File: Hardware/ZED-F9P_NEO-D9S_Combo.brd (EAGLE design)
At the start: 43.2 x 63.5 mm, 179 parts, among them J1 ANTENNA-SMA-GROUNDEDEDGE_SMA, J2 Qwiic Right Angle, J4 Qwiic Right Angle, U1 U-BLOX_NEO-D9S-00B, U2 3.3V, U4 U-BLOX_ZED-F9P, U5 ESD Diode, U6 ESD Diode

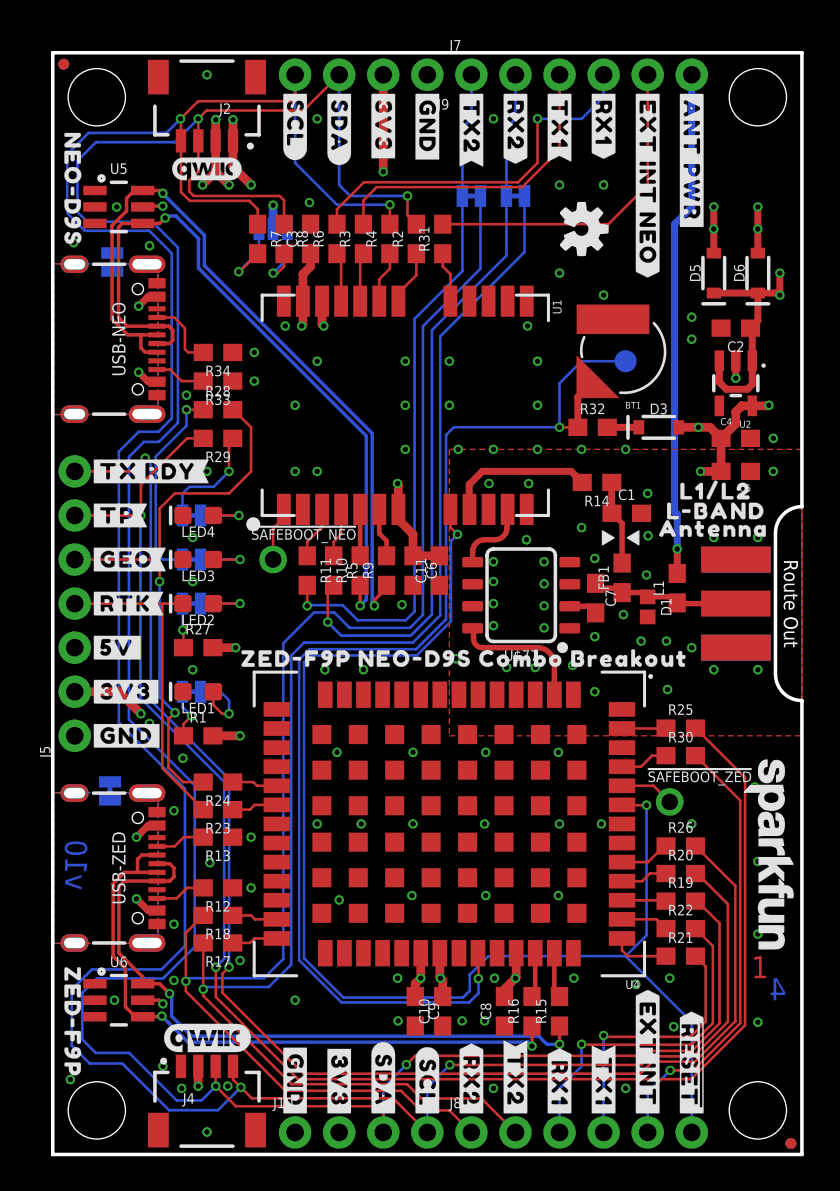
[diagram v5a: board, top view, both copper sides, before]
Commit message: Adds a few vias, fixes some ground pour
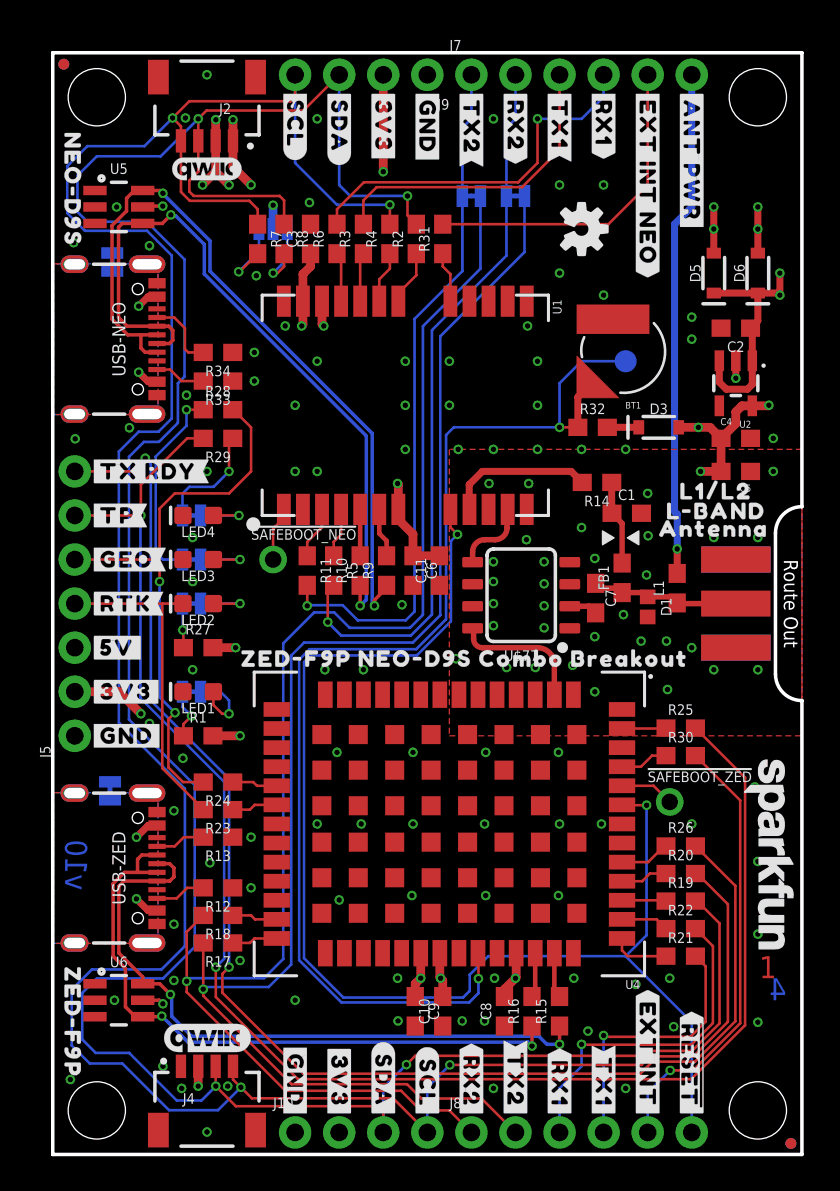
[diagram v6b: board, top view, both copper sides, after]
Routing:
- net GND: vias 123 -> 128

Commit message: Updates note for USB 90 Ohm impedance calculation
* Moves all silk out towards the PTH's
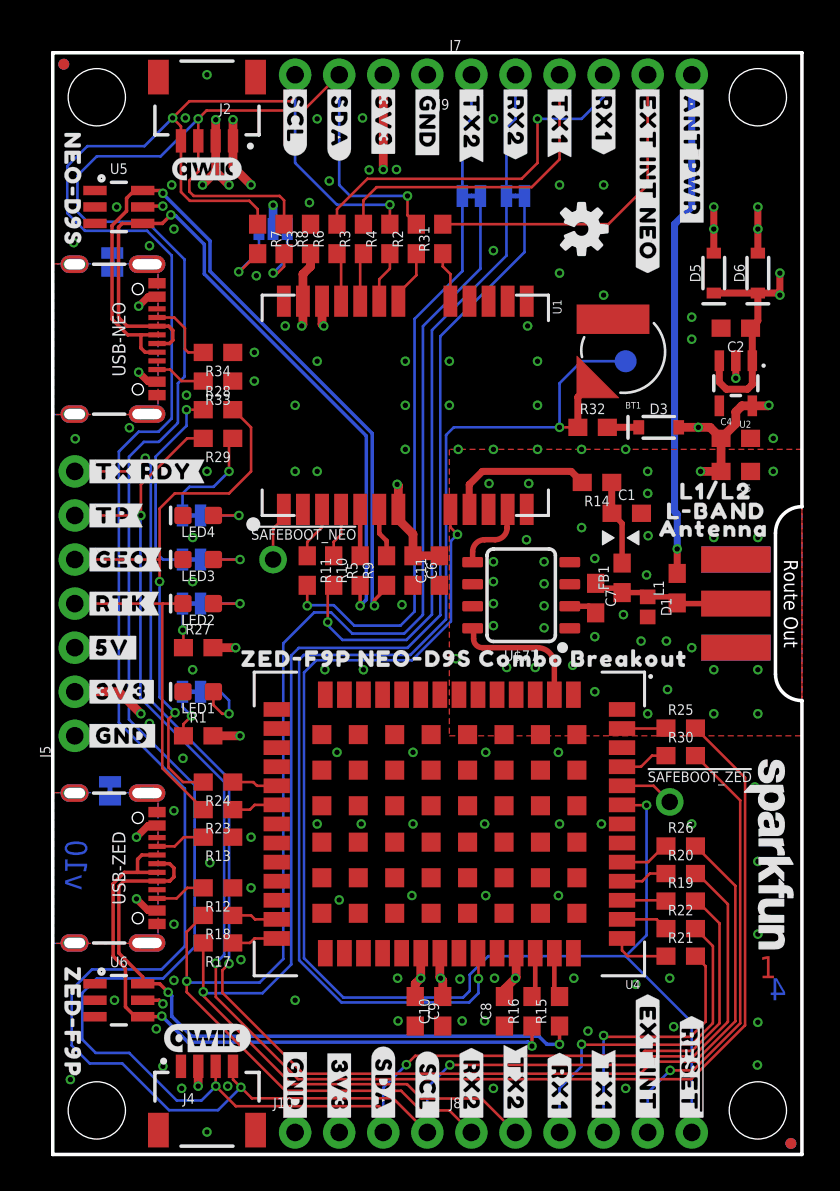
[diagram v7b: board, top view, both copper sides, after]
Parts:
- moved U$10 0.25 mm to (19.1, 1.78)
- moved U$11 0.25 mm to (19.1, 1.78)
- moved U$16 0.25 mm to (1.78, 31.8)
- moved U$17 0.25 mm to (1.78, 31.8)
- moved U$18 0.25 mm to (1.78, 34.3)
- moved U$19 0.25 mm to (1.78, 34.3)
- moved U$2 0.25 mm to (1.78, 24.1)
- moved U$20 0.25 mm to (1.78, 29.2)
- moved U$21 0.25 mm to (1.78, 29.2)
- moved U$23 0.25 mm to (16.5, 1.78)
- moved U$25 0.25 mm to (16.5, 1.78)
- moved U$26 0.25 mm to (1.78, 36.8)
- moved U$27 0.25 mm to (1.78, 36.8)
- moved U$28 0.25 mm to (1.78, 39.4)
- moved U$29 0.25 mm to (1.78, 39.4)
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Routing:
- net GND: vias 128 -> 142

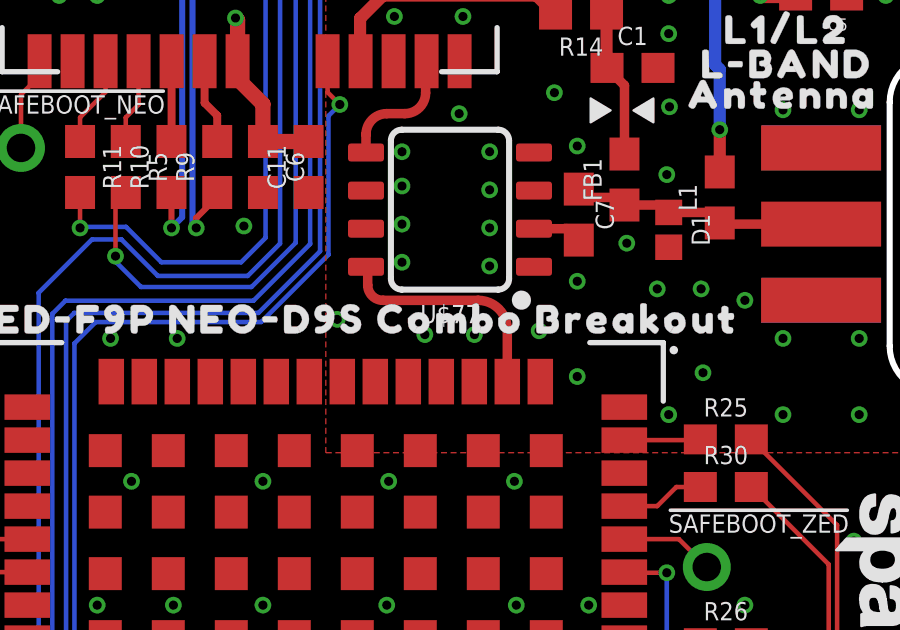
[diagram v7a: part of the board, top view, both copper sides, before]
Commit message: Updates BP2G1+ with minor corrections
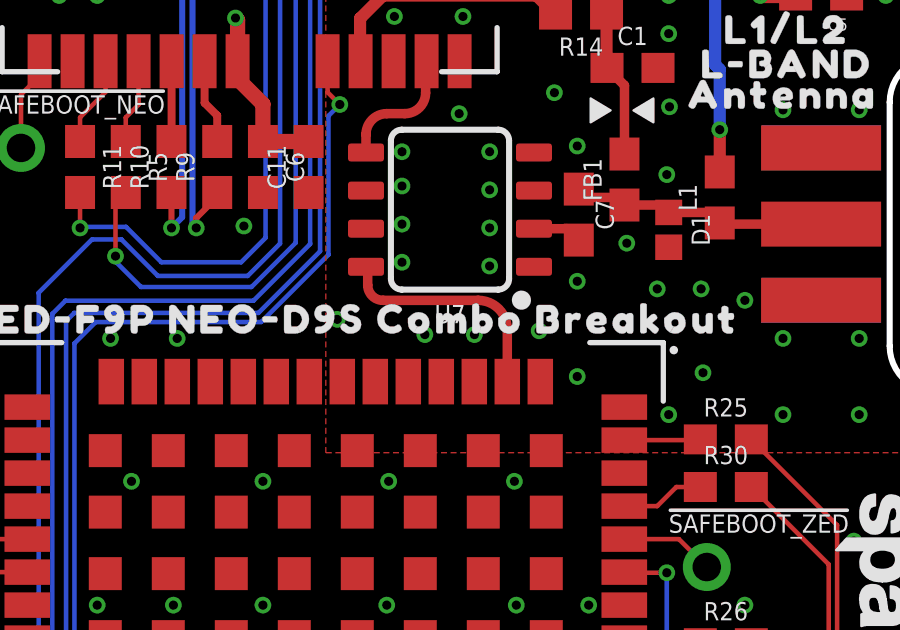
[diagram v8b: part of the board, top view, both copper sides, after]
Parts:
- renumbered U$77 to U7
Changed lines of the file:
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@@
 <attribute name="VALUE" x="3.81" y="6.35" size="0.6096" layer="27" font="vector" ratio="20" align="bottom-center"/>
 </element>
-<element name="U$77" library="SparkFun-RF" package="XX21" value="BP2G1+_POWER_SPLITTER" x="27.0002" y="32.2326" smashed="yes" rot="R90">
+<element name="U7" library="SparkFun-RF" package="XX21" value="BP2G1+_POWER_SPLITTER" x="27.0002" y="32.2326" smashed="yes" rot="R90">
 <attribute name="NAME" x="27.0002" y="29.0576" size="0.6096" layer="25" font="vector" ratio="20" rot="R180" align="bottom-center"/>
 <attribute name="PROD_ID" value="IC-17198" x="27.0002" y="32.2326" size="1.778" layer="27" font="vector" ratio="15" rot="R90" display="off"/>
@@
 <contactref element="U5" pad="2"/>
 <contactref element="U6" pad="2"/>
-<contactref element="U$77" pad="1"/>
-<contactref element="U$77" pad="6"/>
-<contactref element="U$77" pad="3"/>
-<contactref element="U$77" pad="7"/>
-<contactref element="U$77" pad="4"/>
+<contactref element="U7" pad="1"/>
+<contactref element="U7" pad="6"/>
+<contactref element="U7" pad="3"/>
+<contactref element="U7" pad="7"/>
+<contactref element="U7" pad="4"/>
 <via x="25.4" y="34.163" extent="1-16" drill="0.3048"/>
 <via x="28.321" y="31.623" extent="1-16" drill="0.3048"/>
@@
 <signal name="ANT">
 <contactref element="C7" pad="2"/>
-<contactref element="U$77" pad="2"/>
+<contactref element="U7" pad="2"/>
 <wire x1="29.8002" y1="31.5976" x2="30.9127" y2="31.5976" width="0.3175" layer="1"/>
 <wire x1="30.9127" y1="31.5976" x2="31.2928" y2="31.2175" width="0.3175" layer="1"/>
@@
 <contactref element="U1" pad="11"/>
 <wire x1="26.1874" y1="37.1474" x2="26.22" y2="37.18" width="0.3175" layer="1"/>
-<contactref element="U$77" pad="5"/>
+<contactref element="U7" pad="5"/>
 <wire x1="26.1874" y1="36.1248" x2="26.1874" y2="37.1474" width="0.3175" layer="1"/>
 <wire x1="24.2002" y1="34.1376" x2="24.2002" y2="34.7412" width="0.3175" layer="1"/>
@@
 <wire x1="28.91" y1="26.5" x2="28.91" y2="28.24" width="0.3175" layer="1"/>
 <wire x1="28.91" y1="28.24" x2="27.94" y2="29.21" width="0.3175" layer="1" curve="90"/>
-<contactref element="U$77" pad="8"/>
+<contactref element="U7" pad="8"/>
 <wire x1="24.765" y1="29.21" x2="24.257" y2="29.718" width="0.3175" layer="1" curve="-90"/>
 <wire x1="24.257" y1="29.718" x2="24.257" y2="30.2708" width="0.3175" layer="1"/>
